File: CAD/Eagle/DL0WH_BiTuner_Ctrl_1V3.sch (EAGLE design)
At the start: 156 parts, among them Q0321 ABS07-32.768KHZ, U0101 STM32L476RGT6_64PIN_LDO, U0601 MC33996, U0701 MC33996, U0801 MC33996, U0921 TS5A23166, U0941 LM2611, U0951 OPA354, U0961 OPA354, U0962 MCP4661-103E-MS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

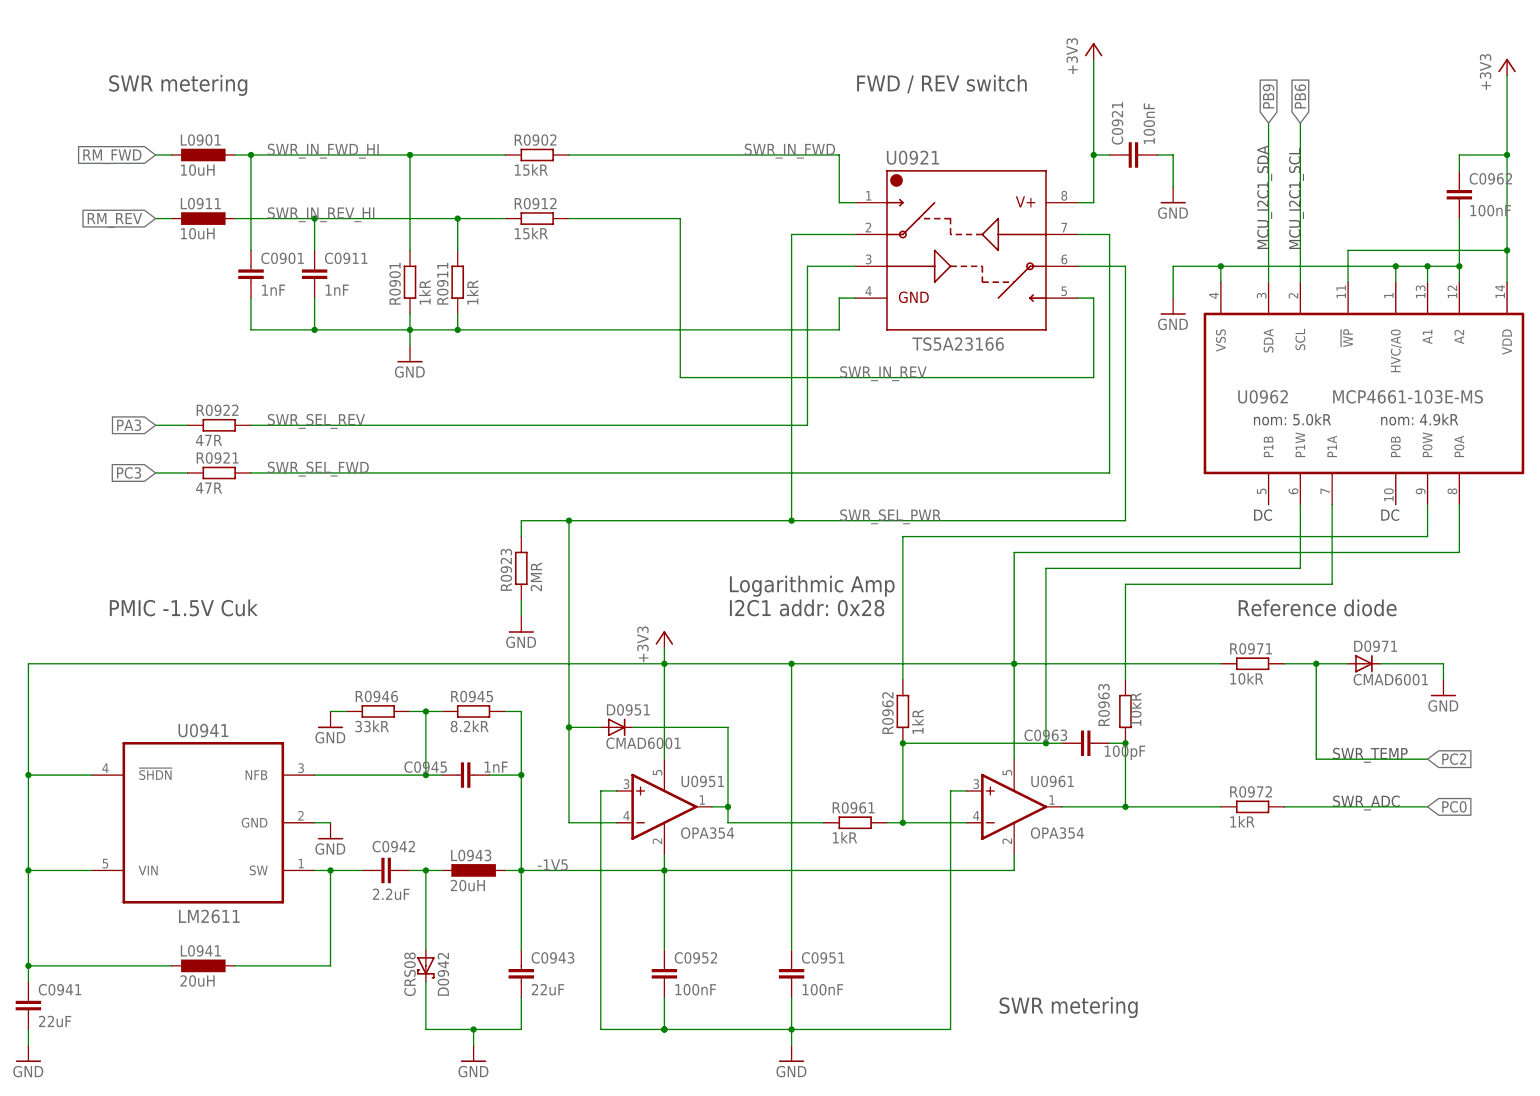
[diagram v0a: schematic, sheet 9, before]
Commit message: HW_1V2,HW_1V3 - CAD/Eagle - voltage divider added to tolerate voltages 0V..10V
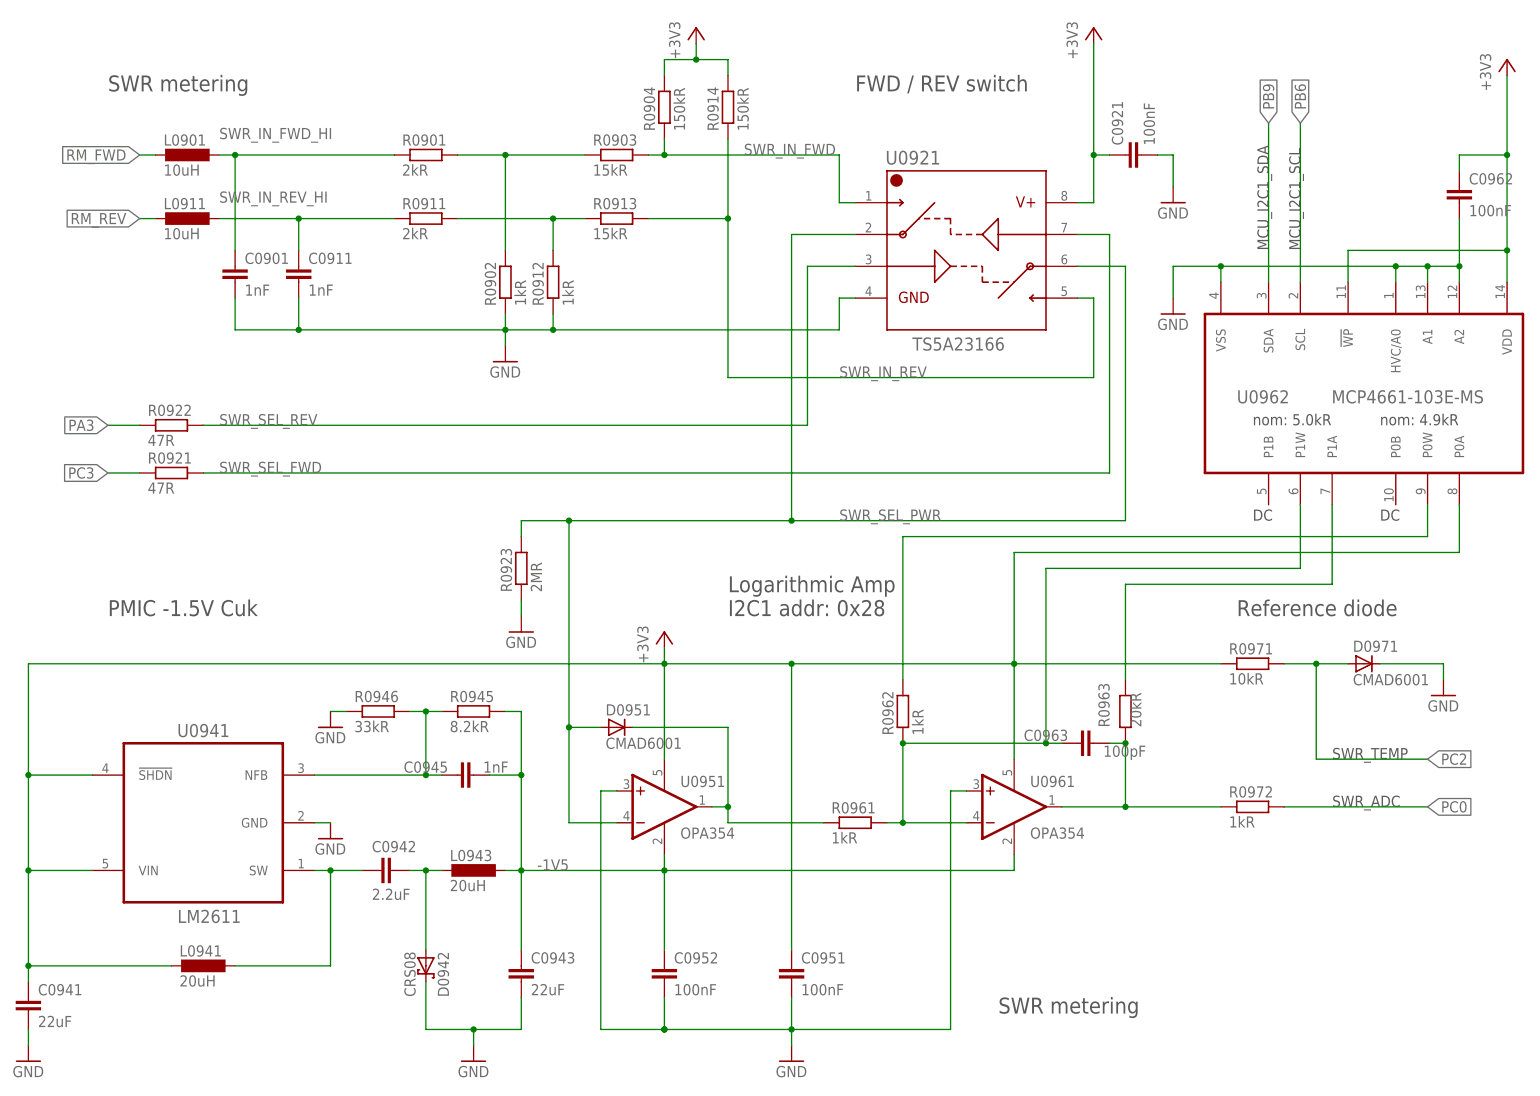
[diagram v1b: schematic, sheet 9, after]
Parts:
- added R0903, R0913: 15kR, df4iah_rcl:R-EU_R0402
- added R0904, R0914: 150kR, df4iah_rcl:R-EU_R0402
- R0901, R0911: value 1kR -> 2kR
- R0902, R0912: value 15kR -> 1kR
- R0963: value 10kR -> 20kR
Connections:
- new net SWR_IN_FWD_LO: R0901.2, R0902.2, R0903.1
- new net SWR_IN_REV_LO: R0911.2, R0912.2, R0913.1
- net +3V3: now also R0904.2, R0914.2
- net GND: now also R0902.1, R0912.1; no longer R0901.1, R0911.1
- net SWR_IN_FWD: now also R0903.2, R0904.1; no longer R0902.2
- net SWR_IN_FWD_HI: now also R0901.1; no longer R0901.2, R0902.1
- net SWR_IN_REV: now also R0913.2, R0914.1; no longer R0912.2
- net SWR_IN_REV_HI: now also R0911.1; no longer R0911.2, R0912.1
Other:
- moved on the sheet: C0901, C0911, L0901, L0911, R0901, R0902, R0911, R0912, R0921, R0922
